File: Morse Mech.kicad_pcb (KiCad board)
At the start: 2 copper layers, 44 x 28 mm, 23 parts, among them P1 USB_OTG, P2 ICSP, SW1 Gateron Green, U1 EEPROM_SPI, Y1 16MHz

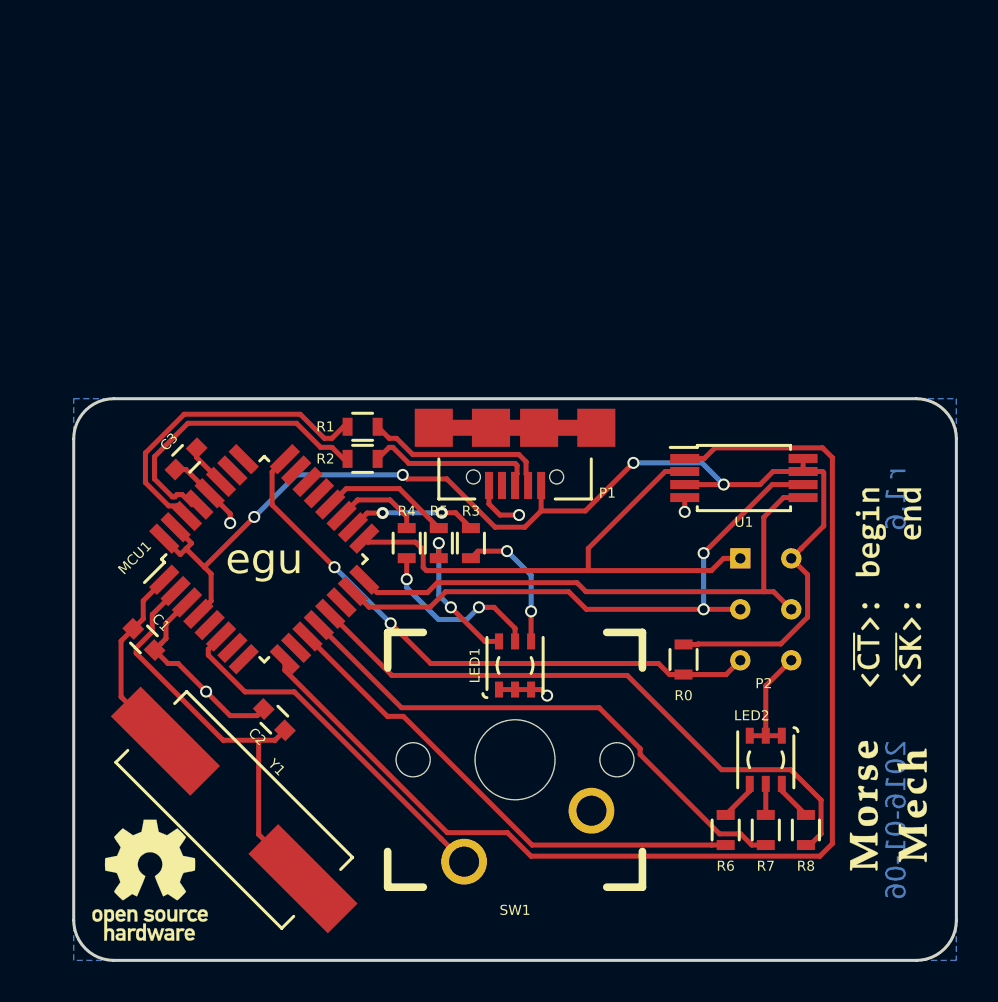
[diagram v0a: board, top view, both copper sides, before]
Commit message: New PCB! (r2.1)
- More compact
- Shorter USB data lines
- Shorter tracks to crystal
- Fewer vias
- Better silkscreen
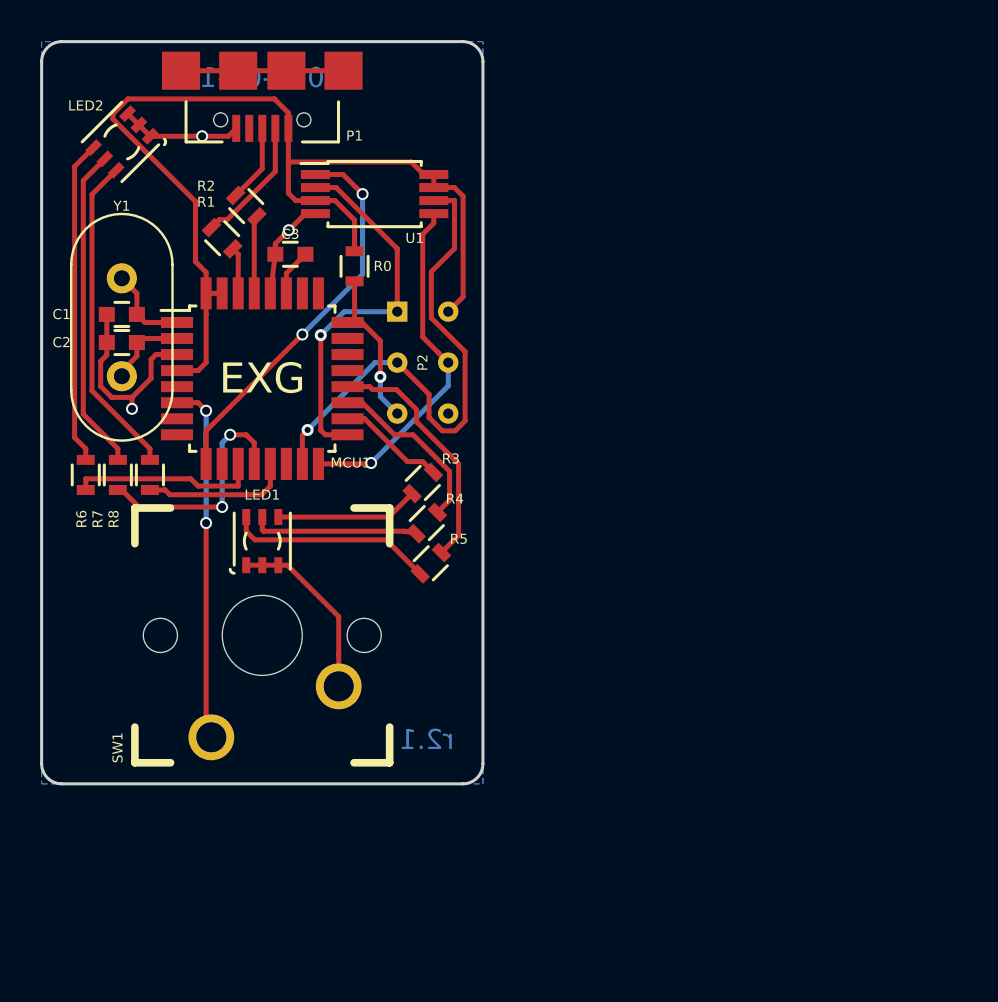
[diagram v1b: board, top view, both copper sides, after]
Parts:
- removed the G*** at (215.0, 127.8)
- G***: value LOGO -> LOGO_MORSE_MECH; moved to B.Cu
- REF***: value OSHW-Logo_5.7x6mm -> OSHW-Logo_5.7x6mm_SilkScreen; moved to B.Cu
- Y1: footprint Crystals:Crystal_HC49-SD_SMD -> Crystals:Crystal_HC49-U_Vertical
- moved LED2 44.5 mm to (214.0, 101.0), turned to 225 degrees
- moved G*** 41.9 mm to (221.0, 99.8), turned to 180 degrees
- moved R8 37.2 mm to (215.4, 117.6)
- moved R7 36.8 mm to (213.8, 117.6)
- moved R6 36.5 mm to (212.2, 117.6)
- moved Y1 27.1 mm to (214.0, 107.8), turned to 270 degrees
- moved R0 25.6 mm to (225.6, 107.2)
- moved U1 23.2 mm to (226.6, 103.6)
- moved P1 21.8 mm to (221.0, 96.0)
- moved P2 21.1 mm to (229.0, 112.0)
- moved C2 20.3 mm to (214.0, 111.0), turned to 180 degrees
- moved REF*** 19.4 mm to (221.0, 119.2), turned to 180 degrees
- moved C1 16.2 mm to (214.0, 109.6), turned to 180 degrees
- moved SW1 14.0 mm to (221.0, 125.6)
- moved LED1 14.0 mm to (221.0, 120.9)
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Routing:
- net /SS_EEPROM: track 59.0 -> 19.4 mm, vias 0 -> 2
- net /LED_IND_B: track 31.0 -> 7.38 mm
- net /RESET: track 29.7 -> 8.12 mm, vias 2 -> 1
- net Net-(C2-Pad1): track 21.2 -> 4.07 mm
- net /LED_IND_R: track 25.1 -> 9.41 mm
- net /LED_IND_G: track 27.0 -> 11.7 mm, vias 0 -> 2
- net Net-(LED2-Pad5): track 1.55 -> 16.2 mm
- net Net-(LED2-Pad6): track 2.05 -> 16.2 mm
- net Net-(LED2-Pad4): track 2.05 -> 16.1 mm
- net /USB_D-: track 15.8 -> 2.33 mm
- net /USB_D+: track 15.0 -> 3.87 mm
- net VCC: track 62.3 -> 51.3 mm, vias 4 -> 0
- net /MOSI: track 28.4 -> 17.5 mm, vias 0 -> 1
- net /MISO: track 27.7 -> 18.9 mm, vias 0 -> 1
- net /LED_SW_B: track 6.56 -> 12.3 mm
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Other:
- board size 44 x 28 mm -> 22 x 37 mm
- board text added: "2017-01-15"
- board text added: "erythro.space"
- board text added: "r2.1"
- board text removed: "2016-01-06"
- board text removed: "egu"
- board text removed: "r 1.6"
